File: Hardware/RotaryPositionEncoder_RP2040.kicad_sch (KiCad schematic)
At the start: 74 parts, among them J1 Conn_ABI, J2 Conn_UVW, J4 USB_C_Receptacle_USB2.0, J5 Conn_5VDC, J7 Conn_CAN, J8 Conn_CAN, J9 Conn_01x04_MountingPin, U1 AS5047P, U2 RP2040, U3 M24C02-RMN, U3 RT9013-33GB, U5 TJA1042T, U7 MAX14783ExS, U8 W25Q32JVZP, Y2 Crystal_GND2

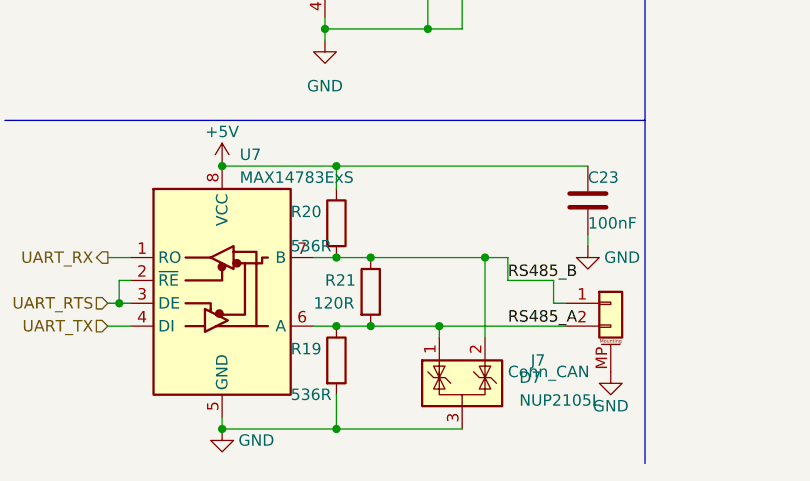
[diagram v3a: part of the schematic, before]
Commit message: Fix: RS485 Pullup/Pulldown Resistor
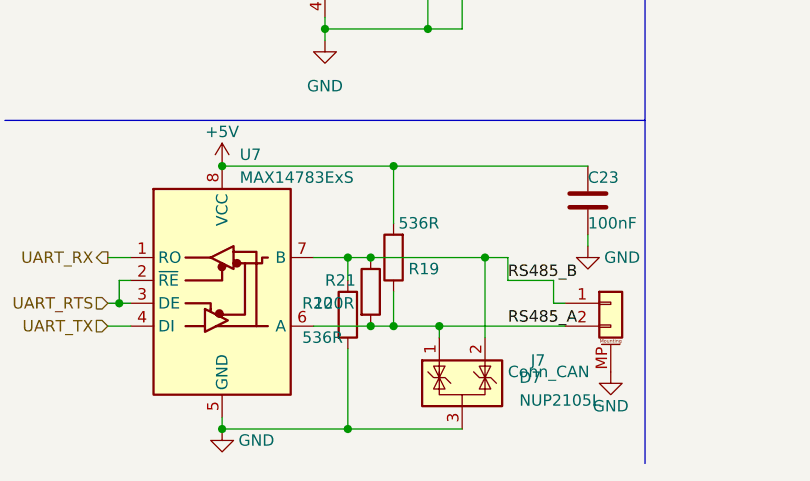
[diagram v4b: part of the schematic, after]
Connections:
- net +5V: now also R19.2; no longer R20.1
- net GND: now also R20.2; no longer R19.2
- net RS485_B: now also R20.1; no longer R20.2
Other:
- moved on the sheet: R19, R20
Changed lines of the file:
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@@
   (junction (at 48.26 149.86) (diameter 0) (color 0 0 0 0)
   )
+  (junction (at 55.88 165.1) (diameter 0) (color 0 0 0 0)
+  )
   (junction (at 66.04 175.26) (diameter 0) (color 0 0 0 0)
   )
@@
   (junction (at 158.75 30.48) (diameter 0) (color 0 0 0 0)
   )
-  (junction (at 49.53 194.31) (diameter 0) (color 0 0 0 0)
-  )
   (junction (at 201.93 33.02) (diameter 0) (color 0 0 0 0)
   )
@@
   (junction (at 149.86 22.86) (diameter 0) (color 0 0 0 0)
   )
-  (junction (at 116.84 78.74) (diameter 0) (color 0 0 0 0)
+  (junction (at 55.88 182.88) (diameter 0) (color 0 0 0 0)
   )
-  (junction (at 49.53 165.1) (diameter 0) (color 0 0 0 0)
+  (junction (at 116.84 78.74) (diameter 0) (color 0 0 0 0)
   )
   (junction (at 237.49 114.3) (diameter 0) (color 0 0 0 0)
@@
   (junction (at 212.09 33.02) (diameter 0) (color 0 0 0 0)
   )
-  (junction (at 49.53 175.26) (diameter 0) (color 0 0 0 0)
-  )
   (junction (at 191.77 22.86) (diameter 0) (color 0 0 0 0)
   )
@@
   (junction (at 207.01 22.86) (diameter 0) (color 0 0 0 0)
   )
+  (junction (at 50.8 194.31) (diameter 0) (color 0 0 0 0)
+  )
   (junction (at 262.89 60.96) (diameter 0) (color 0 0 0 0)
   )
@@
   (junction (at 243.84 29.21) (diameter 0) (color 0 0 0 0)
   )
+  (junction (at 50.8 175.26) (diameter 0) (color 0 0 0 0)
+  )
   (junction (at 21.59 53.34) (diameter 0) (color 0 0 0 0)
   )
@@
   (junction (at 213.36 58.42) (diameter 0) (color 0 0 0 0)
   )
-  (junction (at 49.53 182.88) (diameter 0) (color 0 0 0 0)
-  )
   (no_connect (at 189.23 67.31))
   (no_connect (at 189.23 115.57))
@@
     (stroke (width 0) (type default))
   )
+  (wire (pts (xy 55.88 165.1) (xy 77.47 165.1))
+    (stroke (width 0) (type default))
+  )
   (wire (pts (xy 60.96 182.88) (xy 74.93 182.88))
     (stroke (width 0) (type default))
@@
     (stroke (width 0) (type default))
   )
+  (wire (pts (xy 55.88 182.88) (xy 60.96 182.88))
+    (stroke (width 0) (type default))
+  )
   (wire (pts (xy 186.69 22.86) (xy 191.77 22.86))
     (stroke (width 0) (type default))
@@
     (stroke (width 0) (type default))
   )
-  (wire (pts (xy 49.53 175.26) (xy 53.34 175.26))
+  (wire (pts (xy 46.99 175.26) (xy 50.8 175.26))
     (stroke (width 0) (type default))
   )
@@
     (stroke (width 0) (type default))
   )
-  (wire (pts (xy 77.47 165.1) (xy 49.53 165.1))
+  (wire (pts (xy 36.83 165.1) (xy 55.88 165.1))
     (stroke (width 0) (type default))
   )
@@
     (stroke (width 0) (type default))
   )
+  (wire (pts (xy 50.8 175.26) (xy 50.8 177.8))
+    (stroke (width 0) (type default))
+  )
   (wire (pts (xy 62.23 45.72) (xy 64.77 45.72))
     (stroke (width 0) (type default))
@@
     (stroke (width 0) (type default))
   )
-  (wire (pts (xy 49.53 182.88) (xy 53.34 182.88))
-    (stroke (width 0) (type default))
-  )
   (wire (pts (xy 24.13 175.26) (xy 26.67 175.26))
     (stroke (width 0) (type default))
@@
     (stroke (width 0) (type default))
   )
+  (wire (pts (xy 55.88 179.07) (xy 55.88 182.88))
+    (stroke (width 0) (type default))
+  )
   (wire (pts (xy 173.99 30.48) (xy 173.99 31.75))
     (stroke (width 0) (type default))
@@
     (stroke (width 0) (type default))
   )
+  (wire (pts (xy 53.34 182.88) (xy 55.88 182.88))
+    (stroke (width 0) (type default))
+  )
   (polyline (pts (xy 228.6 12.7) (xy 228.6 97.79))
     (stroke (width 0) (type default))
@@
     (stroke (width 0) (type default))
   )
-  (wire (pts (xy 118.11 86.36) (xy 118.11 85.09))
+  (wire (pts (xy 55.88 165.1) (xy 55.88 171.45))
     (stroke (width 0) (type default))
   )
-  (wire (pts (xy 49.53 190.5) (xy 49.53 194.31))
+  (wire (pts (xy 118.11 86.36) (xy 118.11 85.09))
     (stroke (width 0) (type default))
   )
@@
     (stroke (width 0) (type default))
   )
+  (wire (pts (xy 50.8 185.42) (xy 50.8 194.31))
+    (stroke (width 0) (type default))
+  )
+  (wire (pts (xy 50.8 194.31) (xy 63.5 194.31))
+    (stroke (width 0) (type default))
+  )
   (wire (pts (xy 31.75 143.51) (xy 38.1 143.51))
     (stroke (width 0) (type default))
@@
     (stroke (width 0) (type default))
   )
-  (wire (pts (xy 49.53 165.1) (xy 36.83 165.1))
-    (stroke (width 0) (type default))
-  )
   (wire (pts (xy 68.58 100.33) (xy 68.58 102.87))
     (stroke (width 0) (type default))
@@
     (stroke (width 0) (type default))
   )
-  (wire (pts (xy 53.34 182.88) (xy 60.96 182.88))
-    (stroke (width 0) (type default))
-  )
   (wire (pts (xy 59.69 140.97) (xy 59.69 143.51))
     (stroke (width 0) (type default))
@@
     (stroke (width 0) (type default))
   )
-  (wire (pts (xy 49.53 194.31) (xy 63.5 194.31))
+  (wire (pts (xy 36.83 194.31) (xy 50.8 194.31))
     (stroke (width 0) (type default))
   )
@@
     (stroke (width 0) (type default))
   )
-  (wire (pts (xy 49.53 165.1) (xy 49.53 167.64))
-    (stroke (width 0) (type default))
-  )
   (wire (pts (xy 54.61 106.68) (xy 57.15 106.68))
     (stroke (width 0) (type default))
@@
     (stroke (width 0) (type default))
   )
-  (wire (pts (xy 46.99 182.88) (xy 49.53 182.88))
+  (wire (pts (xy 46.99 182.88) (xy 53.34 182.88))
     (stroke (width 0) (type default))
   )
@@
     (stroke (width 0) (type default))
   )
+  (wire (pts (xy 50.8 175.26) (xy 53.34 175.26))
+    (stroke (width 0) (type default))
+  )
   (wire (pts (xy 62.23 114.3) (xy 62.23 109.22))
     (stroke (width 0) (type default))
@@
     (stroke (width 0) (type default))
   )
-  (wire (pts (xy 46.99 175.26) (xy 49.53 175.26))
-    (stroke (width 0) (type default))
-  )
   (wire (pts (xy 36.83 140.97) (xy 38.1 140.97))
     (stroke (width 0) (type default))
@@
     (stroke (width 0) (type default))
   )
-  (wire (pts (xy 49.53 194.31) (xy 36.83 194.31))
-    (stroke (width 0) (type default))
-  )
   (polyline (pts (xy 228.6 97.79) (xy 284.48 97.79))
     (stroke (width 0) (type default))
@@
     )
   )
-  (symbol (lib_id "Device:R") (at 49.53 186.69 0) (unit 1)
+  (symbol (lib_id "Device:R") (at 55.88 175.26 180) (unit 1)
     (in_bom yes) (on_board yes) (dnp no)
-    (property "Reference" "R19" (at 44.45 185.42 0)
+    (property "Reference" "R19" (at 60.96 176.53 0)
       (effects (font (size 1.27 1.27)) (justify left))
     )
-    (property "Value" "536R" (at 44.45 190.5 0)
+    (property "Value" "536R" (at 60.96 171.45 0)
       (effects (font (size 1.27 1.27)) (justify left))
     )
-    (property "Footprint" "Resistor_SMD:R_0603_1608Metric" (at 47.752 186.69 90)
+    (property "Footprint" "Resistor_SMD:R_0603_1608Metric" (at 57.658 175.26 90)
       (effects (font (size 1.27 1.27)) hide)
     )
-    (property "Datasheet" "~" (at 49.53 186.69 0)
+    (property "Datasheet" "~" (at 55.88 175.26 0)
       (effects (font (size 1.27 1.27)) hide)
     )
@@
     )
   )
-  (symbol (lib_id "Device:R") (at 49.53 171.45 0) (unit 1)
+  (symbol (lib_id "Device:R") (at 50.8 181.61 0) (unit 1)
     (in_bom yes) (on_board yes) (dnp no)
-    (property "Reference" "R20" (at 44.45 170.18 0)
+    (property "Reference" "R20" (at 45.72 180.34 0)
       (effects (font (size 1.27 1.27)) (justify left))
     )
-    (property "Value" "536R" (at 44.45 173.99 0)
+    (property "Value" "536R" (at 45.72 184.15 0)
       (effects (font (size 1.27 1.27)) (justify left))
     )
-    (property "Footprint" "Resistor_SMD:R_0603_1608Metric" (at 47.752 171.45 90)
+    (property "Footprint" "Resistor_SMD:R_0603_1608Metric" (at 49.022 181.61 90)
       (effects (font (size 1.27 1.27)) hide)
     )
-    (property "Datasheet" "~" (at 49.53 171.45 0)
+    (property "Datasheet" "~" (at 50.8 181.61 0)
       (effects (font (size 1.27 1.27)) hide)
     )

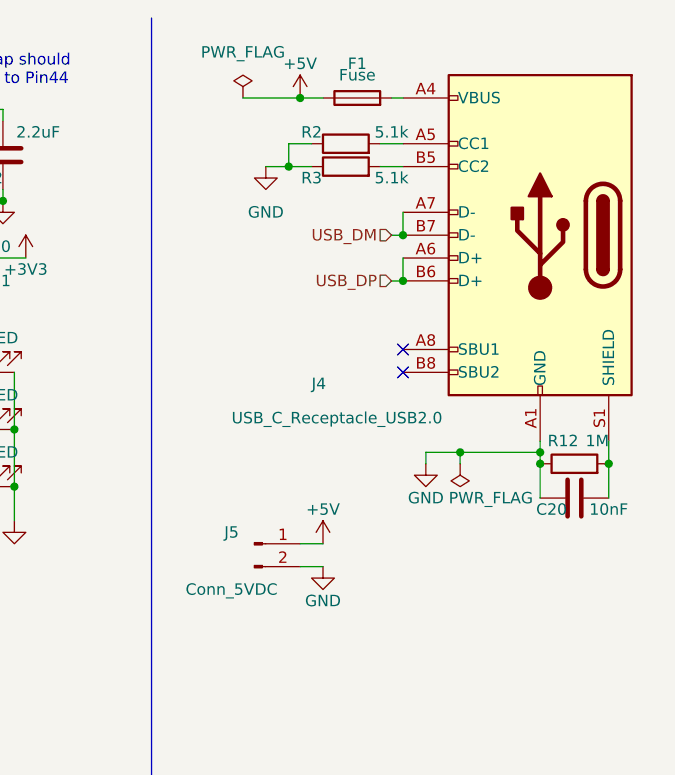
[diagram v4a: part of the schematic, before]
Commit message: Changed USB-C Plug into GH1.25 Connector to take less space
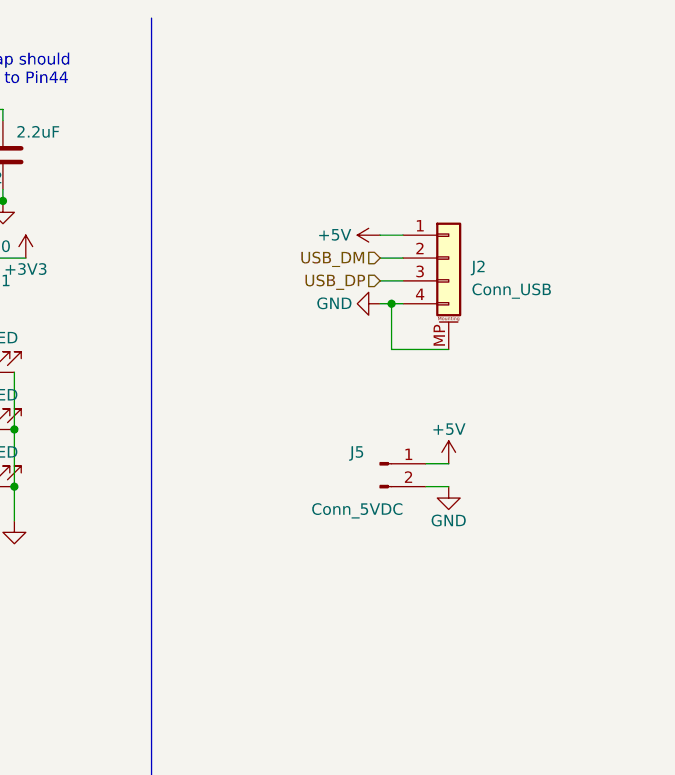
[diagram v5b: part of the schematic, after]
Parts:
- removed C20: 10nF, Capacitor_SMD:C_0603_1608Metric, symbol Device:C
- removed F1: Fuse, Fuse:Fuse_1210_3225Metric, symbol Device:Fuse
- removed J4: USB_C_Receptacle_USB2.0, Connector_USB:USB_C_Receptacle_HRO_TYPE-C-31-M-12, symbol Connector:USB_C_Receptacle_USB2.0
- removed R12: 1M, Resistor_SMD:R_0603_1608Metric, symbol Device:R
- removed R2, R3: 5.1k, Resistor_SMD:R_0603_1608Metric, symbol Device:R
- added J2: Conn_USB, Connector_JST:JST_GH_SM04B-GHS-TB_1x04-1MP_P1.25mm_Horizontal, symbol Connector_Generic_MountingPin:Conn_01x04_MountingPin
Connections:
- net +5V: now also J2.1 (Pin_1)
- net GND: now also J2.4 (Pin_4), J2.MP (MountPin)
- net USB_DM: now also J2.2 (Pin_2)
- net USB_DP: now also J2.3 (Pin_3)
- no-connect marks 24 -> 22
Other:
- moved on the sheet: J5
